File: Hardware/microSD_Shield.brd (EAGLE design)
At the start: 53.3 x 59.7 mm, 19 parts, among them J1 AVR_SPI_PRG_6NS, U1 USD-SOCKETNEW, U2 ARDUINO_R3_SHIELDNOLABELS, U3 HEX_CONVERTER

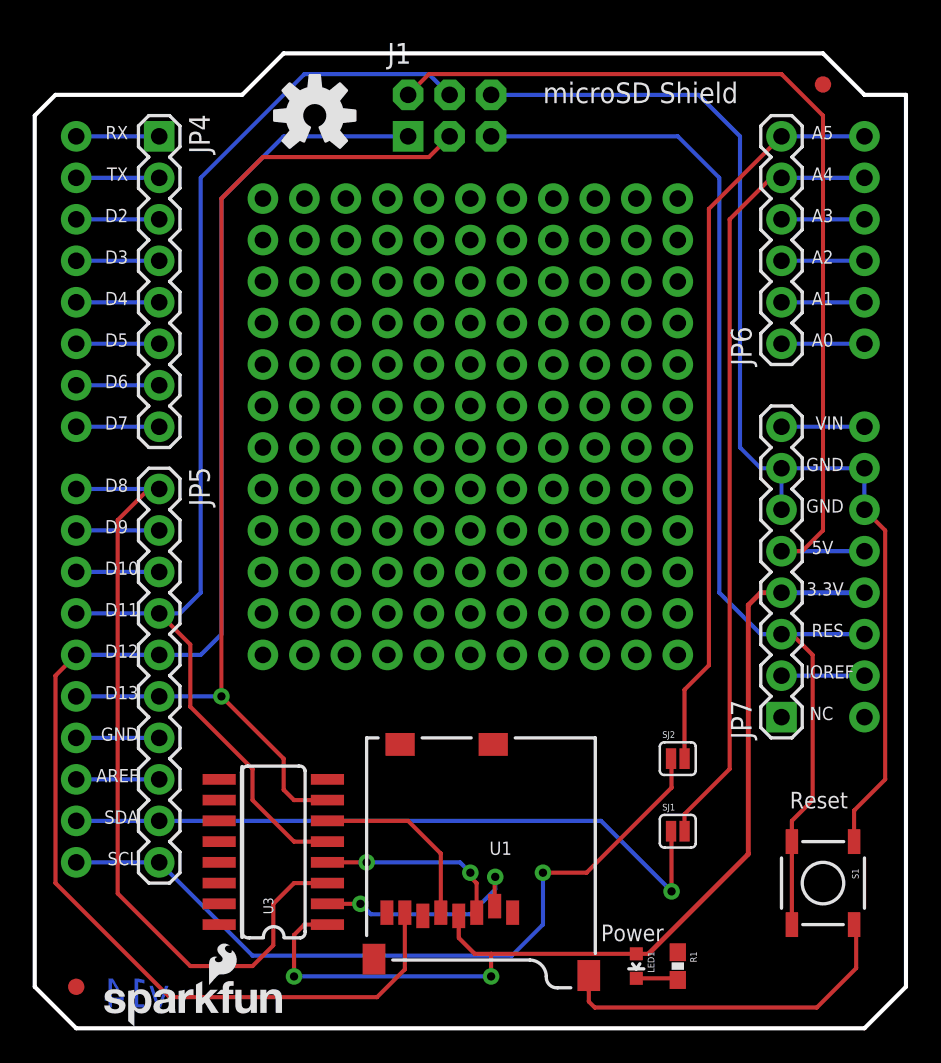
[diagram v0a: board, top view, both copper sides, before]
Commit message: Adding decoupling capacitors
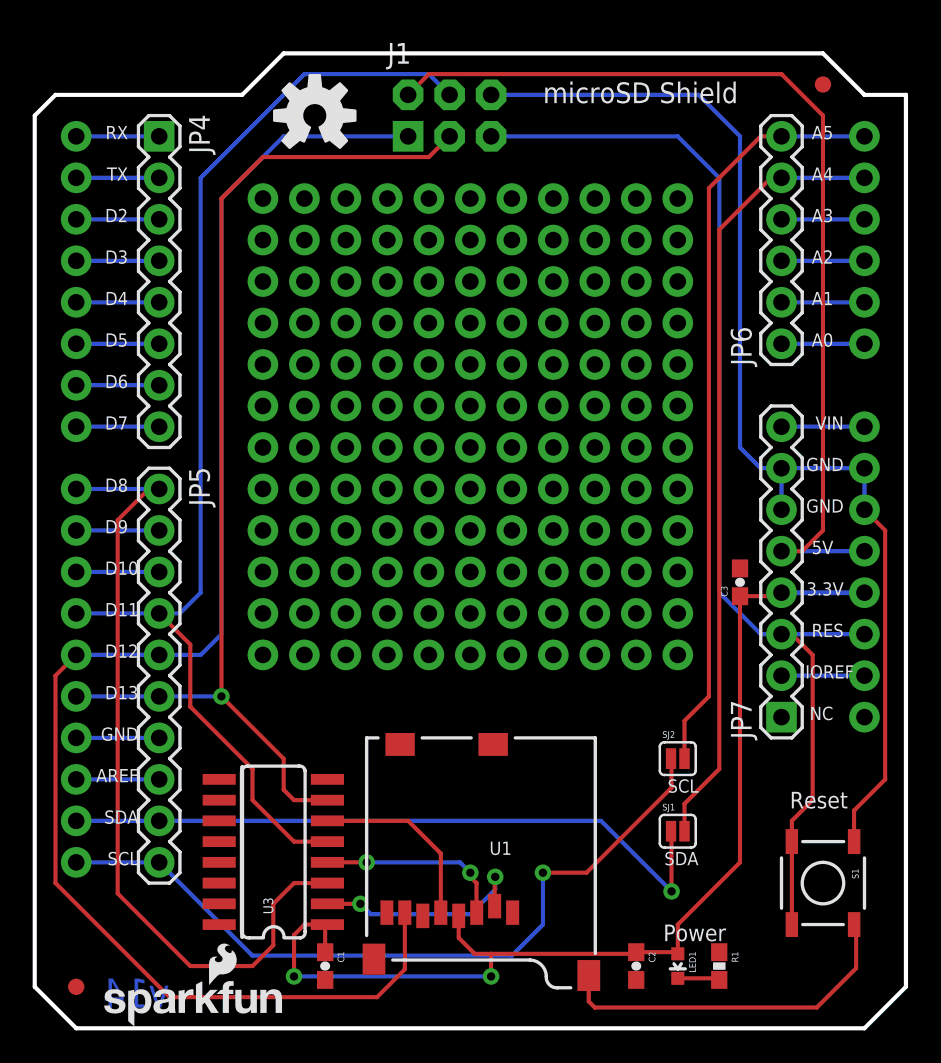
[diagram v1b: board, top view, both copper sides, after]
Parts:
- added C1, C2: 0.1uF, SparkFun-Capacitors:0603-CAP
- added C3: 10uF, SparkFun-Capacitors:0603-CAP
- moved LED1 2.54 mm to (38.1, 3.81)
- moved R1 2.54 mm to (40.6, 3.81)
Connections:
- net 3.3V: now also C1.1, C2.1, C3.1
- net GND: now also C1.2, C2.2, C3.2
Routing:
- net 3.3V: track 63.0 -> 66.5 mm
- net A5: track 45.6 -> 46.4 mm
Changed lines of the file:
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@@
 <?xml version="1.0" encoding="utf-8"?>
 <!DOCTYPE eagle SYSTEM "eagle.dtd">
-<eagle version="6.4">
+<eagle version="6.5.0">
 <drawing>
 <settings>
@@
 <layer number="106" name="bPlate" color="7" fill="1" visible="no" active="yes"/>
 <layer number="107" name="Crop" color="7" fill="1" visible="no" active="yes"/>
-<layer number="108" name="tplace-old" color="10" fill="1" visible="yes" active="yes"/>
-<layer number="109" name="ref-old" color="11" fill="1" visible="yes" active="yes"/>
+<layer number="108" name="tplace-old" color="10" fill="1" visible="no" active="yes"/>
+<layer number="109" name="ref-old" color="11" fill="1" visible="no" active="yes"/>
 <layer number="116" name="Patch_BOT" color="9" fill="4" visible="no" active="yes"/>
 <layer number="121" name="_tsilk" color="7" fill="1" visible="no" active="yes"/>
@@
 <layer number="144" name="Drill_legend" color="7" fill="1" visible="no" active="yes"/>
 <layer number="151" name="HeatSink" color="7" fill="1" visible="no" active="yes"/>
-<layer number="199" name="Contour" color="7" fill="1" visible="yes" active="yes"/>
+<layer number="199" name="Contour" color="7" fill="1" visible="no" active="yes"/>
 <layer number="200" name="200bmp" color="1" fill="10" visible="no" active="yes"/>
 <layer number="201" name="201bmp" color="2" fill="10" visible="no" active="yes"/>
@@
 <wire x1="49.53" y1="57.15" x2="52.07" y2="57.15" width="0.254" layer="20"/>
 <wire x1="11.43" y1="5.588" x2="11.43" y2="16.002" width="0.254" layer="21"/>
-<text x="33.401" y="5.334" size="1.016" layer="21" font="vector" ratio="15">Power</text>
+<text x="37.211" y="5.334" size="1.016" layer="21" font="vector" ratio="15">Power</text>
 <text x="29.845" y="56.642" size="1.27" layer="21" font="vector" ratio="15" rot="SR0">microSD Shield</text>
 <text x="6.985" y="1.27" size="1.778" layer="16" font="vector" ratio="15" rot="MR0">v14</text>
@@
 <text x="24.13" y="-25.4" size="1.27" layer="51" font="vector" ratio="15">Ryan Owens</text>
 <text x="24.13" y="-27.94" size="1.27" layer="51" font="vector" ratio="15">Toni Klopfenstein</text>
+<text x="39.37" y="15.24" size="0.8128" layer="21" font="vector" ratio="20" rot="R180">SCL</text>
+<text x="39.37" y="10.795" size="0.8128" layer="21" font="vector" ratio="20" rot="R180">SDA</text>
 </plain>
 <attributes>
@@
 <element name="U1" library="SparkFun" package="MICRO-SD-SOCKET-PP" value="USD-SOCKETNEW" x="19.05" y="17.78" rot="R180"/>
 <element name="S1" library="SparkFun" package="TACTILE_SWITCH_SMD" value="" x="46.99" y="8.89" rot="R270"/>
-<element name="LED1" library="SparkFun" package="LED-0603" value="Red" x="35.56" y="3.81" rot="R180"/>
-<element name="R1" library="SparkFun" package="0603-RES" value="1k" x="38.1" y="3.81" rot="R270"/>
+<element name="LED1" library="SparkFun" package="LED-0603" value="Red" x="38.1" y="3.81" rot="R180"/>
+<element name="R1" library="SparkFun" package="0603-RES" value="1k" x="40.64" y="3.81" rot="R270"/>
 <element name="JP4" library="SparkFun" package="1X08" value="" x="6.35" y="54.61" rot="R270"/>
 <element name="JP5" library="SparkFun-Connectors" package="1X10" value="M10&quot;" x="6.35" y="33.02" rot="R270"/>
@@
 <element name="SJ2" library="SparkFun-Passives" package="SJ_2S" value="SOLDERJUMPERNC" x="38.1" y="16.51"/>
 <element name="J1" library="SparkFun-Connectors" package="2X3-NS" value="AVR_SPI_PRG_6NS" x="24.13" y="55.88"/>
+<element name="C1" library="SparkFun-Capacitors" package="0603-CAP" value="0.1uF" x="16.51" y="3.81" rot="R270">
+<attribute name="PROD_ID" value="CAP-08604" x="16.51" y="3.81" size="1.778" layer="27" font="vector" ratio="15" rot="R270" display="off"/>
+</element>
+<element name="C2" library="SparkFun-Capacitors" package="0603-CAP" value="0.1uF" x="35.56" y="3.81" rot="R270">
+<attribute name="PROD_ID" value="CAP-08604" x="35.56" y="3.81" size="1.778" layer="27" font="vector" ratio="15" rot="R270" display="off"/>
+</element>
+<element name="C3" library="SparkFun-Capacitors" package="0603-CAP" value="10uF" x="41.91" y="27.305" rot="R90">
+<attribute name="PROD_ID" value="CAP-11015" x="41.91" y="27.305" size="1.778" layer="27" font="vector" ratio="15" rot="R90" display="off"/>
+</element>
 </elements>
 <signals>
@@
 <contactref element="LED1" pad="A"/>
 <contactref element="U3" pad="1"/>
-<wire x1="42.418" y1="10.668" x2="42.418" y2="25.908" width="0.3048" layer="1"/>
-<wire x1="35.56" y1="4.56" x2="36.31" y2="4.56" width="0.254" layer="1"/>
-<wire x1="36.31" y1="4.56" x2="42.418" y2="10.668" width="0.3048" layer="1"/>
 <contactref element="U2" pad="3.3V"/>
 <contactref element="JP7" pad="4"/>
 <wire x1="44.45" y1="26.67" x2="49.53" y2="26.67" width="0.3048" layer="16"/>
-<wire x1="42.418" y1="25.908" x2="43.18" y2="26.67" width="0.3048" layer="1"/>
-<wire x1="43.18" y1="26.67" x2="44.45" y2="26.67" width="0.3048" layer="1"/>
 <wire x1="24.69" y1="6.88" x2="24.69" y2="5.536" width="0.254" layer="1"/>
 <wire x1="24.69" y1="5.536" x2="25.666" y2="4.56" width="0.254" layer="1"/>
-<wire x1="35.56" y1="4.56" x2="26.67" y2="4.56" width="0.254" layer="1"/>
 <wire x1="26.67" y1="4.56" x2="25.666" y2="4.56" width="0.254" layer="1"/>
 <wire x1="16.6497" y1="6.35" x2="15.24" y2="6.35" width="0.254" layer="1"/>
@@
 <via x="26.67" y="3.175" extent="1-16" drill="0.508"/>
 <wire x1="26.67" y1="3.175" x2="26.67" y2="4.56" width="0.254" layer="1"/>
+<contactref element="C2" pad="1"/>
+<contactref element="C1" pad="1"/>
+<contactref element="C3" pad="1"/>
+<wire x1="26.67" y1="4.56" x2="35.46" y2="4.56" width="0.254" layer="1"/>
+<wire x1="35.46" y1="4.56" x2="35.56" y2="4.66" width="0.254" layer="1"/>
+<wire x1="35.56" y1="4.66" x2="38" y2="4.66" width="0.254" layer="1"/>
+<wire x1="38" y1="4.66" x2="38.1" y2="4.56" width="0.254" layer="1"/>
+<wire x1="38.1" y1="4.56" x2="38.1" y2="6.35" width="0.254" layer="1"/>
+<wire x1="16.51" y1="4.66" x2="16.51" y2="6.2103" width="0.254" layer="1"/>
+<wire x1="16.51" y1="6.2103" x2="16.6497" y2="6.35" width="0.254" layer="1"/>
+<wire x1="41.91" y1="26.455" x2="44.235" y2="26.455" width="0.254" layer="1"/>
+<wire x1="44.235" y1="26.455" x2="44.45" y2="26.67" width="0.254" layer="1"/>
+<wire x1="41.91" y1="26.455" x2="41.91" y2="10.16" width="0.254" layer="1"/>
+<wire x1="41.91" y1="10.16" x2="38.1" y2="6.35" width="0.254" layer="1"/>
 </signal>
 <signal name="GND">
@@
 <wire x1="44.45" y1="31.75" x2="44.45" y2="33.655" width="0.254" layer="16"/>
 <wire x1="44.45" y1="33.655" x2="45.085" y2="34.29" width="0.254" layer="16"/>
+<contactref element="C2" pad="2"/>
+<contactref element="C1" pad="2"/>
+<contactref element="C3" pad="2"/>
 </signal>
 <signal name="N$6">
 <contactref element="LED1" pad="C"/>
 <contactref element="R1" pad="2"/>
-<wire x1="38.1" y1="3.175" x2="38.1" y2="2.96" width="0.254" layer="1"/>
-<wire x1="35.56" y1="3.06" x2="37.985" y2="3.06" width="0.254" layer="1"/>
-<wire x1="37.985" y1="3.06" x2="38.1" y2="3.175" width="0.254" layer="1"/>
+<wire x1="38.1" y1="3.06" x2="40.54" y2="3.06" width="0.254" layer="1"/>
+<wire x1="40.54" y1="3.06" x2="40.64" y2="2.96" width="0.254" layer="1"/>
 </signal>
 <signal name="N$7">
@@
 <wire x1="44.45" y1="52.07" x2="49.53" y2="52.07" width="0.254" layer="16"/>
 <contactref element="SJ1" pad="2"/>
-<wire x1="44.45" y1="52.07" x2="43.815" y2="52.07" width="0.254" layer="1"/>
-<wire x1="43.815" y1="52.07" x2="41.275" y2="49.53" width="0.254" layer="1"/>
-<wire x1="41.275" y1="49.53" x2="41.275" y2="15.875" width="0.254" layer="1"/>
-<wire x1="38.5119" y1="12.065" x2="38.5119" y2="13.1119" width="0.254" layer="1"/>
-<wire x1="38.5119" y1="13.1119" x2="41.275" y2="15.875" width="0.254" layer="1"/>
+<wire x1="38.5119" y1="12.065" x2="38.5119" y2="13.7469" width="0.254" layer="1"/>
+<wire x1="38.5119" y1="13.7469" x2="40.64" y2="15.875" width="0.254" layer="1"/>
+<wire x1="40.64" y1="15.875" x2="40.64" y2="48.895" width="0.254" layer="1"/>
+<wire x1="40.64" y1="48.895" x2="43.815" y2="52.07" width="0.254" layer="1"/>
+<wire x1="43.815" y1="52.07" x2="44.45" y2="52.07" width="0.254" layer="1"/>
 </signal>
 <signal name="A5">
@@
 <wire x1="44.45" y1="54.61" x2="49.53" y2="54.61" width="0.254" layer="16"/>
 <contactref element="SJ2" pad="2"/>
-<wire x1="38.5119" y1="16.51" x2="38.5119" y2="20.7319" width="0.254" layer="1"/>
-<wire x1="38.5119" y1="20.7319" x2="40.005" y2="22.225" width="0.254" layer="1"/>
-<wire x1="40.005" y1="22.225" x2="40.005" y2="50.165" width="0.254" layer="1"/>
-<wire x1="40.005" y1="50.165" x2="44.45" y2="54.61" width="0.254" layer="1"/>
+<wire x1="43.18" y1="54.61" x2="44.45" y2="54.61" width="0.254" layer="1"/>
+<wire x1="43.18" y1="54.61" x2="40.005" y2="51.435" width="0.254" layer="1"/>
+<wire x1="40.005" y1="51.435" x2="40.005" y2="20.32" width="0.254" layer="1"/>
+<wire x1="38.5119" y1="16.51" x2="38.5119" y2="18.8269" width="0.254" layer="1"/>
+<wire x1="38.5119" y1="18.8269" x2="40.005" y2="20.32" width="0.254" layer="1"/>
 </signal>
 <signal name="RES">

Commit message: Adding bottom flame to pcb
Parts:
- added LOGO2: SFE_LOGO_FLAME.1_INCH, SparkFun-Aesthetics:SFE_LOGO_FLAME_.1

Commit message: Upping back flame size
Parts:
- LOGO2: value SFE_LOGO_FLAME.1_INCH -> SFE_LOGO_FLAME.6_INCH; device SparkFun-Aesthetics:SFE_LOGO_FLAME_.1 -> SparkFun-Aesthetics:SFE_LOGO_FLAME_.6
- moved LOGO2 12.5 mm to (31.8, 2.54)
